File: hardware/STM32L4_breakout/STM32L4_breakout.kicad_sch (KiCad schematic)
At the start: 64 parts, among them J1 12V IN, J10 GPIO, J11 SPI1, J12 USART1, J13 USART3, J14 UART4, J15 3.3V, J16 5V, J17 12V, J2 SWD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

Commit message: breakout board PCB layout WIP
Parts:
- removed J2: SWD, Connector_PinHeader_2.54mm:PinHeader_2x05_P2.54mm_Vertical, symbol Connector_Generic:Conn_02x05_Odd_Even
- added J2: SWD, Connector_PinHeader_2.54mm:PinHeader_1x06_P2.54mm_Vertical, symbol Connector_Generic:Conn_01x06
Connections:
- net GND: now also J2.6 (Pin_6)
- net STM_NRST: now also J2.5 (Pin_5)
- net SWCLK: now also J2.3 (Pin_3)
- net SWDIO: now also J2.2 (Pin_2)
- net SWO: now also J2.4 (Pin_4)
- net VMEM: now also J2.1 (Pin_1)
- no-connect marks 33 -> 30

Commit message: breakout board PCB layout WIP
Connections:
- net CARDCS_5V: now also J10.8 (Pin_8); no longer J10.3 (Pin_3)
- net D7: now also J10.7 (Pin_7); no longer J10.4 (Pin_4)
- net RELAY1_CTRL: now also J10.5 (Pin_5); no longer J10.7 (Pin_7)
- net RELAY2_CTRL: now also J10.2 (Pin_2); no longer J10.9 (Pin_9)
- net RT_CS: now also J10.4 (Pin_4); no longer J10.8 (Pin_8)
- net TFT_CS: now also J10.9 (Pin_9); no longer J10.2 (Pin_2)
- net TFT_DC: now also J10.3 (Pin_3); no longer J10.5 (Pin_5)

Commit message: breakout board layout WIP
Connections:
- net I2C_PULL_3V3: now reaches R1.2, R2.1, R3.1, R4.2, R5.1, R6.1
- net ARD_3V3A: now reaches J5.8 (Pin_8), R15.2
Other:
- moved on the sheet: C10, R1, R15, R4

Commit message: breakout board pcb layout WIP
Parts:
- C11, C12: footprint Capacitor_SMD:C_0603_1608Metric -> Capacitor_SMD:C_0402_1005Metric
- J3, J6: footprint Connector_PinHeader_2.54mm:PinHeader_1x08_P2.54mm_Vertical -> Connector_PinSocket_2.54mm:PinSocket_1x08_P2.54mm_Vertical
- J4: footprint Connector_PinHeader_2.54mm:PinHeader_1x06_P2.54mm_Vertical -> Connector_PinSocket_2.54mm:PinSocket_1x06_P2.54mm_Vertical
- J5: footprint Connector_PinHeader_2.54mm:PinHeader_1x10_P2.54mm_Vertical -> Connector_PinSocket_2.54mm:PinSocket_1x10_P2.54mm_Vertical
- R16, R18: footprint Resistor_SMD:R_0603_1608Metric -> Resistor_SMD:R_0402_1005Metric
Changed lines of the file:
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@@
     (property "Reference" "R18" (id 0) (at 127.635 175.26 90))
     (property "Value" "0" (id 1) (at 127.635 177.8 90))
-    (property "Footprint" "Resistor_SMD:R_0603_1608Metric" (id 2) (at 127.381 179.324 90)
+    (property "Footprint" "Resistor_SMD:R_0402_1005Metric" (id 2) (at 127.381 179.324 90)
       (effects (font (size 1.27 1.27)) hide)
     )
@@
       (effects (font (size 1.27 1.27)) hide)
     )
-    (property "Footprint" "Connector_PinHeader_2.54mm:PinHeader_1x08_P2.54mm_Vertical" (id 2) (at 57.785 178.435 0)
+    (property "Footprint" "Connector_PinSocket_2.54mm:PinSocket_1x08_P2.54mm_Vertical" (id 2) (at 57.785 178.435 0)
       (effects (font (size 1.27 1.27)) hide)
     )
@@
       (effects (font (size 1.27 1.27)) (justify left) hide)
     )
-    (property "Footprint" "Connector_PinHeader_2.54mm:PinHeader_1x06_P2.54mm_Vertical" (id 2) (at 48.895 178.435 0)
+    (property "Footprint" "Connector_PinSocket_2.54mm:PinSocket_1x06_P2.54mm_Vertical" (id 2) (at 48.895 178.435 0)
       (effects (font (size 1.27 1.27)) hide)
     )
@@
     (property "Reference" "C11" (id 0) (at 160.02 154.94 90))
     (property "Value" "5.1 pF" (id 1) (at 160.02 157.48 90))
-    (property "Footprint" "Capacitor_SMD:C_0603_1608Metric" (id 2) (at 156.21 161.5948 0)
+    (property "Footprint" "Capacitor_SMD:C_0402_1005Metric" (id 2) (at 156.21 161.5948 0)
       (effects (font (size 1.27 1.27)) hide)
     )
@@
     (property "Reference" "R16" (id 0) (at 127.635 156.845 90))
     (property "Value" "0" (id 1) (at 127.635 159.385 90))
-    (property "Footprint" "Resistor_SMD:R_0603_1608Metric" (id 2) (at 127.381 161.544 90)
+    (property "Footprint" "Resistor_SMD:R_0402_1005Metric" (id 2) (at 127.381 161.544 90)
       (effects (font (size 1.27 1.27)) hide)
     )
@@
     (property "Reference" "C12" (id 0) (at 160.655 184.785 90))
     (property "Value" "5.1 pF" (id 1) (at 160.655 187.325 90))
-    (property "Footprint" "Capacitor_SMD:C_0603_1608Metric" (id 2) (at 156.845 179.3748 0)
+    (property "Footprint" "Capacitor_SMD:C_0402_1005Metric" (id 2) (at 156.845 179.3748 0)
       (effects (font (size 1.27 1.27)) hide)
     )
@@
       (effects (font (size 1.27 1.27)) hide)
     )
-    (property "Footprint" "Connector_PinHeader_2.54mm:PinHeader_1x10_P2.54mm_Vertical" (id 2) (at 57.785 150.495 0)
+    (property "Footprint" "Connector_PinSocket_2.54mm:PinSocket_1x10_P2.54mm_Vertical" (id 2) (at 57.785 150.495 0)
       (effects (font (size 1.27 1.27)) hide)
     )
@@
       (effects (font (size 1.27 1.27)) (justify left) hide)
     )
-    (property "Footprint" "Connector_PinHeader_2.54mm:PinHeader_1x08_P2.54mm_Vertical" (id 2) (at 48.895 150.495 0)
+    (property "Footprint" "Connector_PinSocket_2.54mm:PinSocket_1x08_P2.54mm_Vertical" (id 2) (at 48.895 150.495 0)
       (effects (font (size 1.27 1.27)) hide)
     )
@@
     )
     (path "/a9aaffde-9e56-41c8-8861-003f95c6d254"
-      (reference "C11") (unit 1) (value "5.1 pF") (footprint "Capacitor_SMD:C_0603_1608Metric")
+      (reference "C11") (unit 1) (value "5.1 pF") (footprint "Capacitor_SMD:C_0402_1005Metric")
     )
     (path "/dda582b1-9f1d-4a27-a84e-5df3aae3053b"
-      (reference "C12") (unit 1) (value "5.1 pF") (footprint "Capacitor_SMD:C_0603_1608Metric")
+      (reference "C12") (unit 1) (value "5.1 pF") (footprint "Capacitor_SMD:C_0402_1005Metric")
     )
     (path "/484a3474-4136-4a0e-b3b0-0be99723d52c"
@@
     )
     (path "/e04d0994-9c39-49ca-8beb-73d95c368980"
-      (reference "J3") (unit 1) (value "Conn_01x08") (footprint "Connector_PinHeader_2.54mm:PinHeader_1x08_P2.54mm_Vertical")
+      (reference "J3") (unit 1) (value "Conn_01x08") (footprint "Connector_PinSocket_2.54mm:PinSocket_1x08_P2.54mm_Vertical")
     )
     (path "/8f9a6559-5cf4-431d-b794-a8eeb5d0d272"
-      (reference "J4") (unit 1) (value "Conn_01x06") (footprint "Connector_PinHeader_2.54mm:PinHeader_1x06_P2.54mm_Vertical")
+      (reference "J4") (unit 1) (value "Conn_01x06") (footprint "Connector_PinSocket_2.54mm:PinSocket_1x06_P2.54mm_Vertical")
     )
     (path "/deca5cb1-f877-4330-9af0-dc8b0d15c05e"
-      (reference "J5") (unit 1) (value "Conn_01x10") (footprint "Connector_PinHeader_2.54mm:PinHeader_1x10_P2.54mm_Vertical")
+      (reference "J5") (unit 1) (value "Conn_01x10") (footprint "Connector_PinSocket_2.54mm:PinSocket_1x10_P2.54mm_Vertical")
     )
     (path "/28bc3019-30ac-499b-b265-1b5c1fb4928f"
-      (reference "J6") (unit 1) (value "Conn_01x08") (footprint "Connector_PinHeader_2.54mm:PinHeader_1x08_P2.54mm_Vertical")
+      (reference "J6") (unit 1) (value "Conn_01x08") (footprint "Connector_PinSocket_2.54mm:PinSocket_1x08_P2.54mm_Vertical")
     )
     (path "/8e32aa6d-2c68-4237-8d0a-16559d994f97"
@@
     )
     (path "/c8ca5e13-ce47-47fc-bf42-0c1386fc6746"
-      (reference "R16") (unit 1) (value "0") (footprint "Resistor_SMD:R_0603_1608Metric")
+      (reference "R16") (unit 1) (value "0") (footprint "Resistor_SMD:R_0402_1005Metric")
     )
     (path "/1570c36d-693f-4c10-b56e-b0bb687e7b83"
-      (reference "R18") (unit 1) (value "0") (footprint "Resistor_SMD:R_0603_1608Metric")
+      (reference "R18") (unit 1) (value "0") (footprint "Resistor_SMD:R_0402_1005Metric")
     )
     (path "/06eddd5a-f381-4d52-a6b0-d04d4474ef50"

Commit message: breakout board pcb layout WIP - ready for outline
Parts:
- removed R4: 0 - DNI, Resistor_SMD:R_0603_1608Metric, symbol Device:R_US
- added H1, H2, H3, H4: MountingHole_Pad, MountingHole:MountingHole_3.2mm_M3_DIN965_Pad_TopOnly, symbol Mechanical:MountingHole_Pad
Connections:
- net GND: now also H1.1, H2.1, H3.1, H4.1
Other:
- note added: "Mounting Holes"
- note added: "Option to jump R1 to 5V for all I2C pullups"

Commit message: created PCB outline
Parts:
- SW1: footprint Button_Switch_SMD:SW_SPDT_CK-JS102011SAQN -> Button_Switch_SMD:SW_SPDT_PCM12
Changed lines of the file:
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@@
       (effects (font (size 1.27 1.27)) hide)
     )
-    (property "Footprint" "Button_Switch_SMD:SW_SPDT_CK-JS102011SAQN" (id 2) (at 146.05 69.85 0)
+    (property "Footprint" "Button_Switch_SMD:SW_SPDT_PCM12" (id 2) (at 146.05 69.85 0)
       (effects (font (size 1.27 1.27)) hide)
     )
@@
     )
     (path "/c3e2a4b6-1948-4c98-85ea-7f6f38296147"
-      (reference "SW1") (unit 1) (value "SW_SPDT") (footprint "Button_Switch_SMD:SW_SPDT_CK-JS102011SAQN")
+      (reference "SW1") (unit 1) (value "SW_SPDT") (footprint "Button_Switch_SMD:SW_SPDT_PCM12")
     )
     (path "/1f822ab7-9aa2-4492-a95c-d6a675a300a1"

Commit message: breakout board signal routing WIP
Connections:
- net USART1_RX: now also J12.2 (Pin_2); no longer J12.1 (Pin_1)
- net USART1_TX: now also J12.1 (Pin_1); no longer J12.2 (Pin_2)
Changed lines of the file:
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@@
-    (stroke (width 0) (type default) (color 0 0 0 0))
-  )
-  (wire (pts (xy 264.795 103.505) (xy 260.985 103.505))
     (stroke (width 0) (type default) (color 0 0 0 0))
   )
@@
     (stroke (width 0) (type default) (color 0 0 0 0))
   )
-  (wire (pts (xy 264.795 100.965) (xy 260.985 100.965))
-    (stroke (width 0) (type default) (color 0 0 0 0))
-  )
   (wire (pts (xy 62.865 178.435) (xy 66.04 178.435))
     (stroke (width 0) (type default) (color 0 0 0 0))
@@
     (stroke (width 0) (type default) (color 0 0 0 0))
   )
+  (wire (pts (xy 260.985 100.965) (xy 264.795 100.965))
+    (stroke (width 0) (type default) (color 0 0 0 0))
+  )
   (polyline (pts (xy 104.775 193.675) (xy 174.625 193.675))
     (stroke (width 0) (type default) (color 0 0 0 0))
@@
   )
   (wire (pts (xy 207.01 62.23) (xy 212.09 62.23))
+    (stroke (width 0) (type default) (color 0 0 0 0))
+  )
+  (wire (pts (xy 260.985 103.505) (xy 264.795 103.505))
     (stroke (width 0) (type default) (color 0 0 0 0))
   )
@@
     )
   )
-  (global_label "USART1_TX" (shape input) (at 260.985 103.505 180) (fields_autoplaced)
-    (effects (font (size 1.27 1.27)) (justify right))
-    (property "Intersheet References" "${INTERSHEET_REFS}" (id 0) (at 248.3514 103.4256 0)
+  (global_label "USART1_TX" (shape input) (at 260.985 100.965 180) (fields_autoplaced)
+    (effects (font (size 1.27 1.27)) (justify right))
+    (property "Intersheet References" "${INTERSHEET_REFS}" (id 0) (at 248.3514 100.8856 0)
       (effects (font (size 1.27 1.27)) (justify right) hide)
     )
@@
     )
   )
-  (global_label "USART1_RX" (shape input) (at 260.985 100.965 180) (fields_autoplaced)
-    (effects (font (size 1.27 1.27)) (justify right))
-    (property "Intersheet References" "${INTERSHEET_REFS}" (id 0) (at 248.049 100.8856 0)
-      (effects (font (size 1.27 1.27)) (justify right) hide)
-    )
+  (global_label "USART1_RX" (shape input) (at 260.985 103.505 180) (fields_autoplaced)
+    (effects (font (size 1.27 1.27)) (justify right))
+    (property "Intersheet References" "${INTERSHEET_REFS}" (id 0) (at 248.049 103.4256 0)
+      (effects (font (size 1.27 1.27)) (justify right) hide)
+    )

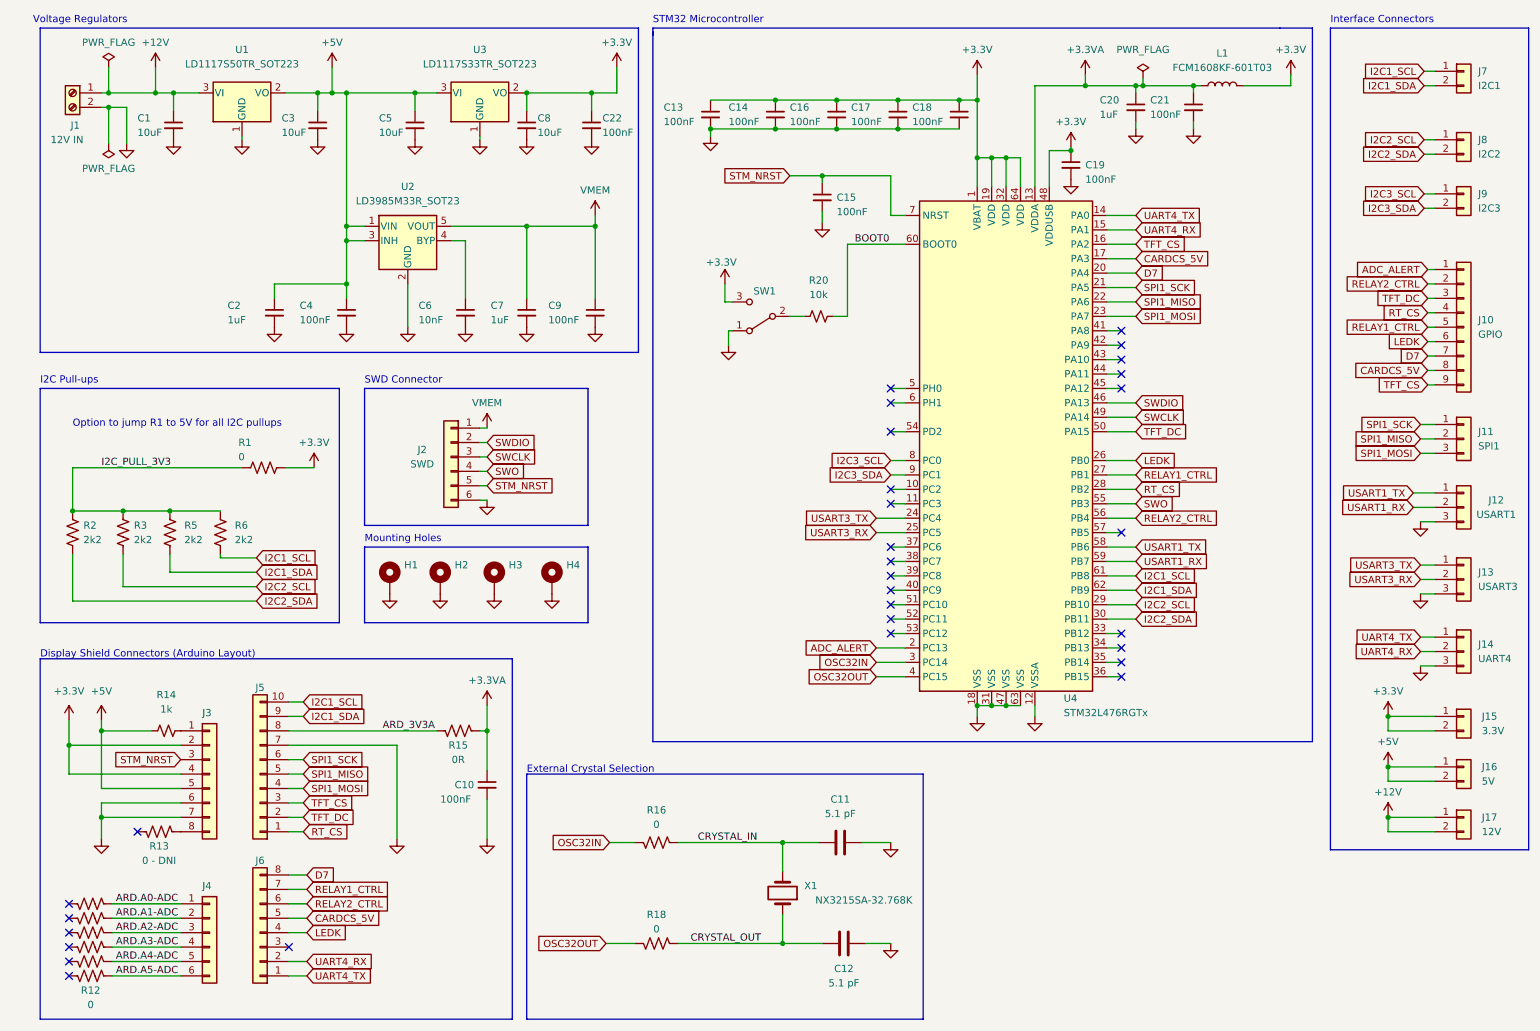
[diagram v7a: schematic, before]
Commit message: added pullups to I2C3
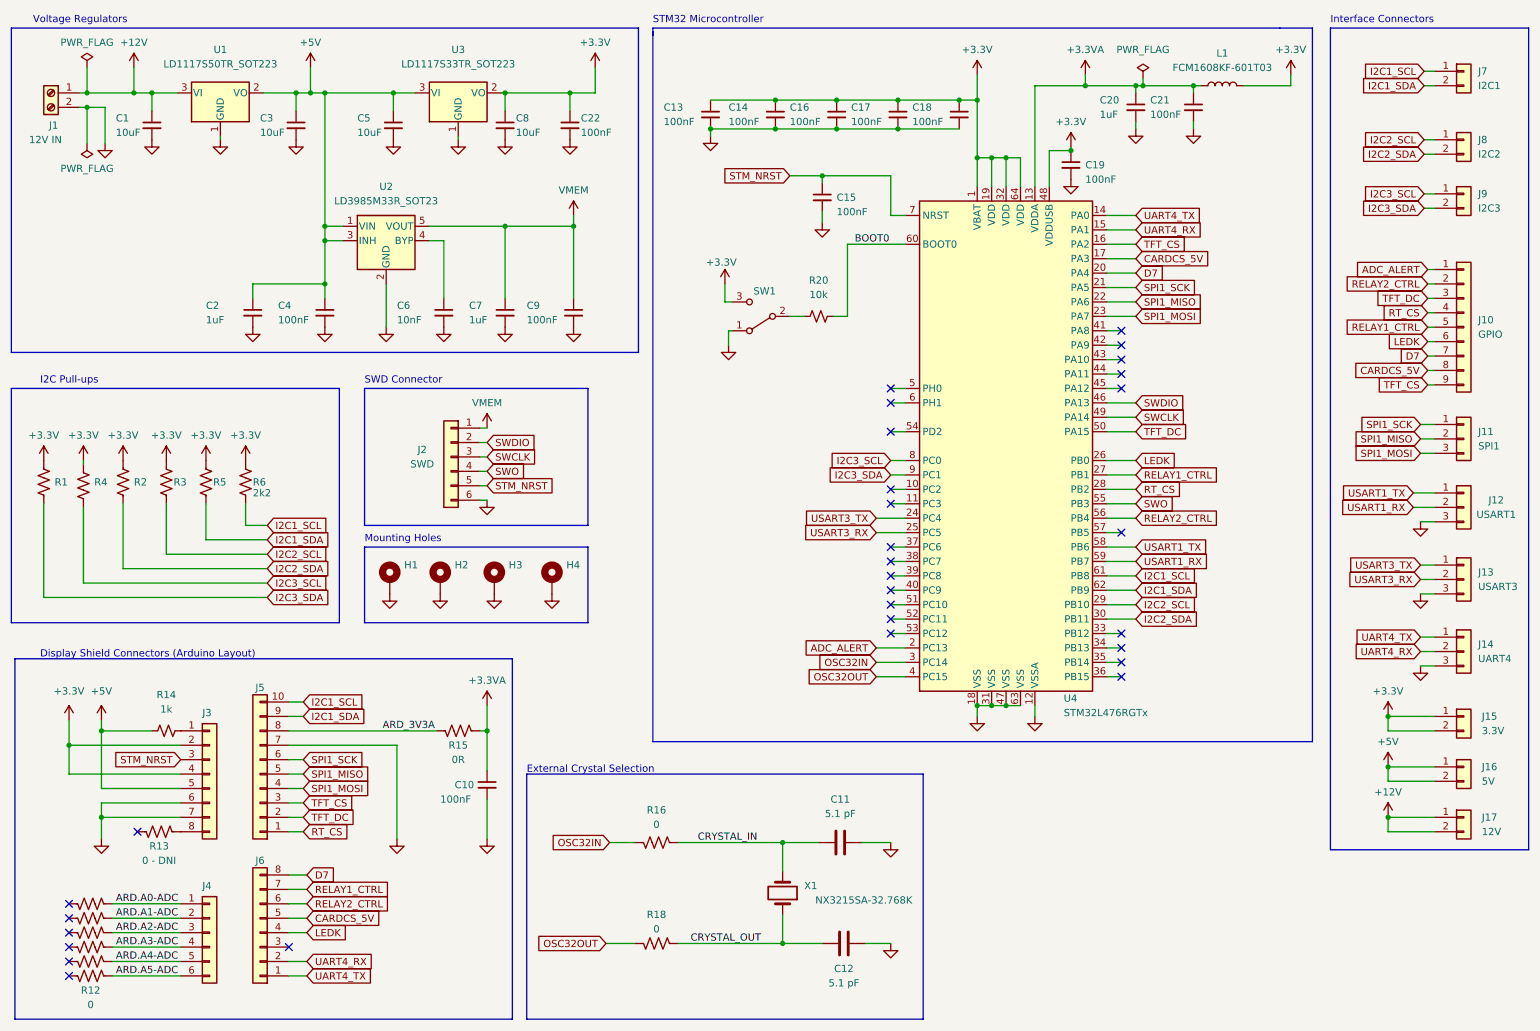
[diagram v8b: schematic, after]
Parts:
- added R4: 2k2, Resistor_SMD:R_0603_1608Metric, symbol Device:R_US
- R1: value 0 -> 2k2
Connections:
- net +3.3V: now also R2.1, R3.1, R5.1, R6.1, R4.1
- net I2C3_SCL: now also R4.2
- net I2C3_SDA: now also R1.2
- removed net I2C_PULL_3V3: R1.2, R2.1, R3.1, R5.1, R6.1
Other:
- note removed: "Option to jump R1 to 5V for all I2C pullups"
- moved on the sheet: C1, C2, C22, C3, C4, C5, C6, C7, C8, C9, J1, R2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
